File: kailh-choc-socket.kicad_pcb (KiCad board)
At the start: 2 copper layers, 18 x 17 mm, 8 parts, among them SW1 SW_DIP_x01

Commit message: Added layer details
M  .gitignore
M  README.md
M  fp-lib-table
M  kailh-choc-socket.kicad_pcb
M  kailh-choc-socket.kicad_prl
M  kailh-choc-socket.kicad_pro
M  kailh-choc-socket.kicad_sch
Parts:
- removed H1, H6: MountingHole_Pad, MountingHole:MountingHole_2.2mm_M2_Pad_Via
- removed H2, H3, H4, H5: MountingHole, MountingHole:MountingHole_2mm
- added J1: Conn_01x01_Male, Giri-Kailh-Choc-Library:TestPoint_THTPad_1.0x1.5mm_Drill0.5mm, F.Cu at (126.4, 69.2)
- added J2: Conn_01x01_Male, Giri-Kailh-Choc-Library:TestPoint_THTPad_1.0x1.5mm_Drill0.5mm, F.Cu at (126.2, 71.5)
- added J3: Conn_01x01_Male, Giri-Kailh-Choc-Library:TestPoint_THTPad_1.0x1.5mm_Drill0.5mm, F.Cu at (112.0, 82.8)
- added J4: Conn_01x01_Male, Giri-Kailh-Choc-Library:TestPoint_THTPad_1.0x1.5mm_Drill0.5mm, F.Cu at (126.2, 73.6)
- added J5: Conn_01x01_Male, Giri-Kailh-Choc-Library:TestPoint_THTPad_1.0x1.5mm_Drill0.5mm, F.Cu at (111.9, 73.6)
- added J6: Conn_01x01_Male, Giri-Kailh-Choc-Library:TestPoint_THTPad_1.0x1.5mm_Drill0.5mm, F.Cu at (111.6, 69.2)
- added J7: Conn_01x01_Male, Giri-Kailh-Choc-Library:TestPoint_THTPad_1.0x1.5mm_Drill0.5mm, F.Cu at (126.3, 82.4)
- added J8: Conn_01x01_Male, Giri-Kailh-Choc-Library:TestPoint_THTPad_1.0x1.5mm_Drill0.5mm, F.Cu at (111.9, 71.5)
- SW1: value SW_DIP_x01 -> SW_DIP_x02; footprint Switch_Keyboard_Hotswap_Kailh:SW_Hotswap_Kailh_Choc_V1_1.00u -> Giri-Kailh-Choc-Library:SW_Hotswap_Kailh_Choc_V1_plated_girish2
- moved SW1 30.3 mm to (119.1, 75.9)
- moved D1 17.5 mm to (123.5, 78.7), turned to 0 degrees
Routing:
- net Net-(J6-Pad1): track 0.00 -> 17.4 mm
- net Net-(J2-Pad1): track 0.00 -> 17.0 mm
- net Net-(J1-Pad1): track 6.76 -> 19.6 mm, vias 0 -> 1
- net Net-(J4-Pad1): track 8.46 -> 20.9 mm
- net Net-(D1-Pad1): track 5.44 -> 3.21 mm
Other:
- board size 18 x 17 mm -> 19 x 18 mm
- board text added: "AmoebaChoc (1.2mm PCB)"
- board text added: "Girish"
- board text added: "Kailh Choc Hotswap"
- board text added: "SMD 6028 Monochorome LED"
- board text added: "SOD-123 Diode"

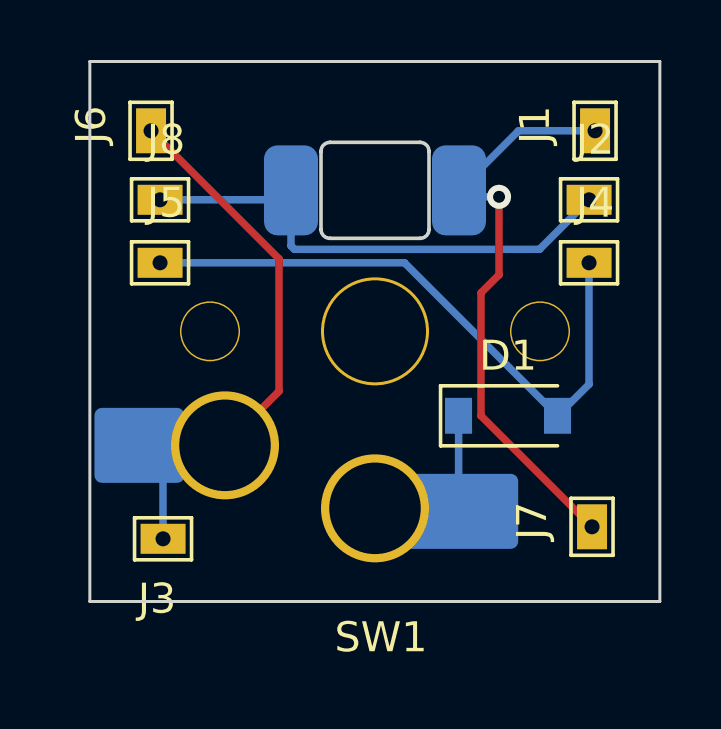
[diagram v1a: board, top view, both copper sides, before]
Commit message: Add new footprints for mounting holes
A  Giri-Kailh-Choc-Library.pretty/D_SOD-123.kicad_mod
A  Giri-Kailh-Choc-Library.pretty/MountingHole_1.2mm_M1.kicad_mod
D  Giri-Kailh-Choc-Library.pretty/SW_Hotswap_Kailh_Choc_V1_plated_girish.kicad_mod
M  Giri-Kailh-Choc-Library.pretty/SW_Hotswap_Kailh_Choc_V1_plated_girish2.kicad_mod
M  Giri-Kailh-Choc-Library.pretty/TestPoint_THTPad_1.0x1.5mm_Drill0.5mm.kicad_mod
A  Giri-Kailh-Choc-Library.pretty/TestPoint_THTPad_1.0x2.5mm_Drill0.5mm.kicad_mod
M  kailh-choc-socket.kicad_pcb
M  kailh-choc-socket.kicad_prl
M  kailh-choc-socket.kicad_sch
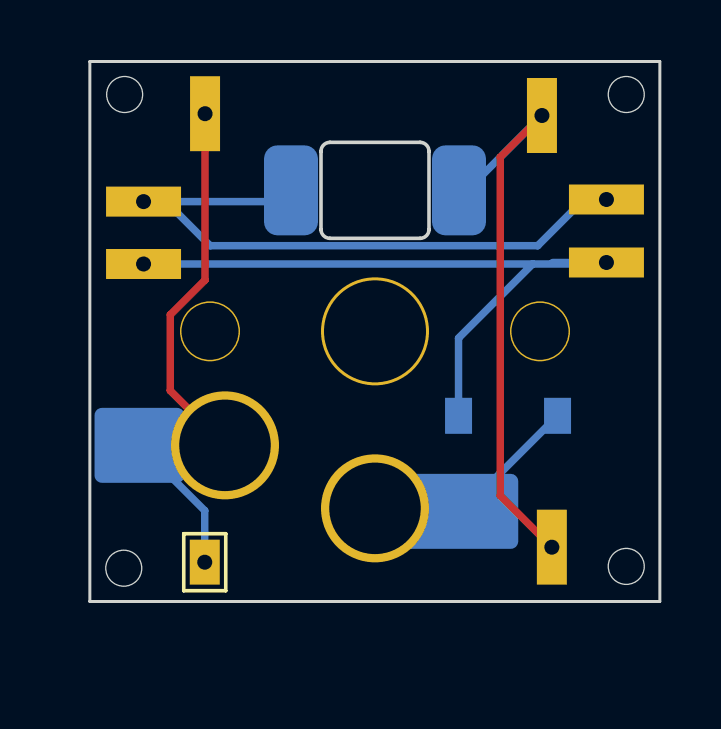
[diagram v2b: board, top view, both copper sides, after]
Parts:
- added H1: MountingHole, Giri-Kailh-Choc-Library:MountingHole_1.2mm_M1, F.Cu at (110.7, 83.8)
- added H2: MountingHole, Giri-Kailh-Choc-Library:MountingHole_1.2mm_M1, F.Cu at (110.7, 68.0)
- added H3: MountingHole, Giri-Kailh-Choc-Library:MountingHole_1.2mm_M1, F.Cu at (127.4, 68.0)
- added H4: MountingHole, Giri-Kailh-Choc-Library:MountingHole_1.2mm_M1, F.Cu at (127.4, 83.7)
- D1: footprint Diode_SMD:D_SOD-123 -> Giri-Kailh-Choc-Library:D_SOD-123; moved to B.Cu
- J1, J2, J4, J5, J6, J7, J8: footprint Giri-Kailh-Choc-Library:TestPoint_THTPad_1.0x1.5mm_Drill0.5mm -> Giri-Kailh-Choc-Library:TestPoint_THTPad_1.0x2.5mm_Drill0.5mm
- moved J6 1.89 mm to (113.4, 68.6)
- moved J1 1.84 mm to (124.6, 68.7)
- moved J3 1.59 mm to (113.4, 83.6), turned to -90 degrees
- moved J7 1.50 mm to (125.0, 83.1)
- moved J2 0.58 mm to (126.8, 71.5)
- moved J4 0.58 mm to (126.8, 73.6)
- moved J8 0.55 mm to (111.3, 71.6)
- moved J5 0.55 mm to (111.3, 73.6)
- turned D1 to 180 degrees
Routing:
- net Net-(J2-Pad1): track 17.0 -> 21.7 mm
- net Net-(D1-Pad2): track 20.9 -> 23.3 mm
- net Net-(D1-Pad1): track 3.21 -> 4.65 mm
- net Net-(J1-Pad1): track 19.6 -> 20.3 mm, vias 1 -> 0
- net Net-(J3-Pad1): track 17.4 -> 18.0 mm
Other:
- board text added: "Column"
- board text added: "Kailh Choc 1350 Hotswap"
- board text added: "LED(A)"
- board text added: "LED(C)"
- board text added: "Row"
- board text removed: "Kailh Choc Hotswap"
